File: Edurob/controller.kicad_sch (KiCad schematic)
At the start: 7 parts, among them SW1 SW_Push, U4 ESP32-S3-WROOM-1

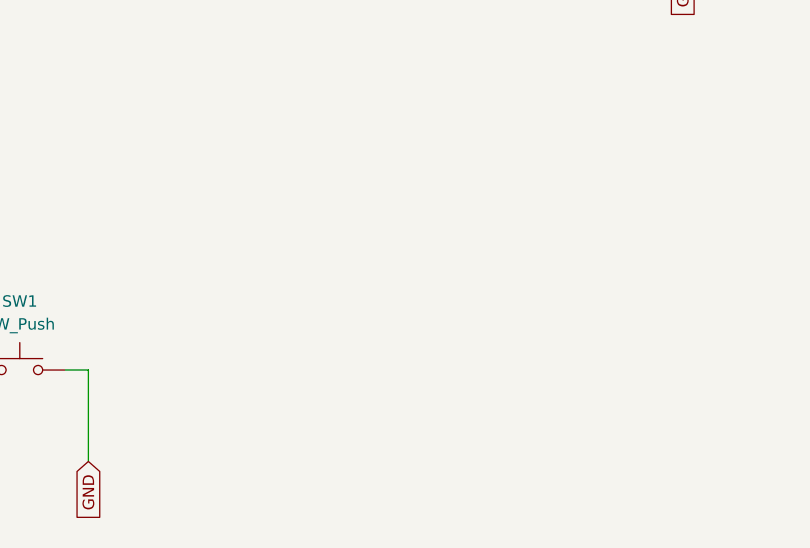
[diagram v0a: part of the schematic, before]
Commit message: Added GPIO Expander, finalized Connector positions
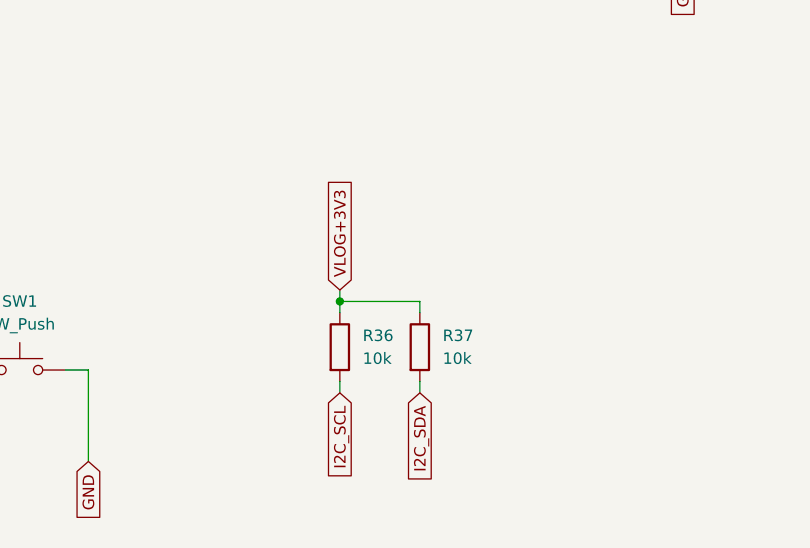
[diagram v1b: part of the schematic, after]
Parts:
- added R36, R37: 10k, Resistor_SMD:R_0603_1608Metric, symbol Device:R
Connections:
- net I2C_SCL: now also R36.2
- net I2C_SDA: now also R37.2
- net VLOG+3V3: now also R36.1, R37.1
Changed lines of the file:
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@@
 (kicad_sch (version 20230121) (generator eeschema)
   (paper "A4")
+  (junction (at 101.6 170.18) (diameter 0) (color 0 0 0 0)
+  )
   (junction (at 17.78 177.8) (diameter 0) (color 0 0 0 0)
   )
@@
     (stroke (width 0) (type default))
   )
+  (wire (pts (xy 101.6 168.91) (xy 101.6 170.18))
+    (stroke (width 0) (type default))
+  )
   (wire (pts (xy 185.42 104.14) (xy 186.69 104.14))
     (stroke (width 0) (type default))
@@
     (stroke (width 0) (type default))
   )
+  (wire (pts (xy 110.49 180.34) (xy 110.49 179.07))
+    (stroke (width 0) (type default))
+  )
   (wire (pts (xy 17.78 186.69) (xy 17.78 187.96))
     (stroke (width 0) (type default))
@@
     (stroke (width 0) (type default))
   )
+  (wire (pts (xy 110.49 171.45) (xy 110.49 170.18))
+    (stroke (width 0) (type default))
+  )
   (wire (pts (xy 185.42 124.46) (xy 186.69 124.46))
     (stroke (width 0) (type default))
@@
     (stroke (width 0) (type default))
   )
+  (wire (pts (xy 101.6 170.18) (xy 101.6 171.45))
+    (stroke (width 0) (type default))
+  )
   (wire (pts (xy 26.67 177.8) (xy 17.78 177.8))
     (stroke (width 0) (type default))
@@
     (stroke (width 0) (type default))
   )
+  (wire (pts (xy 101.6 180.34) (xy 101.6 179.07))
+    (stroke (width 0) (type default))
+  )
   (wire (pts (xy 186.69 53.34) (xy 185.42 53.34))
     (stroke (width 0) (type default))
@@
   )
   (wire (pts (xy 185.42 73.66) (xy 186.69 73.66))
+    (stroke (width 0) (type default))
+  )
+  (wire (pts (xy 110.49 170.18) (xy 101.6 170.18))
     (stroke (width 0) (type default))
   )
@@
     )
   )
+  (global_label "VLOG+3V3" (shape input) (at 101.6 168.91 90) (fields_autoplaced)
+    (effects (font (size 1.27 1.27)) (justify left))
+    (property "Intersheetrefs" "${INTERSHEET_REFS}" (at 101.6 156.1276 90)
+      (effects (font (size 1.27 1.27)) (justify left) hide)
+    )
+  )
+  (global_label "I2C_SDA" (shape input) (at 110.49 180.34 270) (fields_autoplaced)
+    (effects (font (size 1.27 1.27)) (justify right))
+    (property "Intersheetrefs" "${INTERSHEET_REFS}" (at 110.49 190.9452 90)
+      (effects (font (size 1.27 1.27)) (justify right) hide)
+    )
+  )
   (global_label "MOT_B_ENCA" (shape input) (at 186.69 81.28 0) (fields_autoplaced)
     (effects (font (size 1.27 1.27)) (justify left))
@@
     )
   )
+  (global_label "I2C_SCL" (shape input) (at 101.6 180.34 270) (fields_autoplaced)
+    (effects (font (size 1.27 1.27)) (justify right))
+    (property "Intersheetrefs" "${INTERSHEET_REFS}" (at 101.6 190.8847 90)
+      (effects (font (size 1.27 1.27)) (justify right) hide)
+    )
+  )
   (global_label "EspEn" (shape input) (at 26.67 171.45 90) (fields_autoplaced)
     (effects (font (size 1.27 1.27)) (justify left))
@@
     (property "Intersheetrefs" "${INTERSHEET_REFS}" (at 84.6726 53.4194 0)
       (effects (font (size 1.27 1.27)) (justify right) hide)
+    )
+  )
+  (symbol (lib_id "Device:R") (at 101.6 175.26 0) (unit 1)
+    (in_bom yes) (on_board yes) (dnp no) (fields_autoplaced)
+    (property "Reference" "R36" (at 104.14 173.9899 0)
+      (effects (font (size 1.27 1.27)) (justify left))
+    )
+    (property "Value" "10k" (at 104.14 176.5299 0)
+      (effects (font (size 1.27 1.27)) (justify left))
+    )
+    (property "Footprint" "Resistor_SMD:R_0603_1608Metric" (at 99.822 175.26 90)
+      (effects (font (size 1.27 1.27)) hide)
+    )
+    (property "Datasheet" "~" (at 101.6 175.26 0)
+      (effects (font (size 1.27 1.27)) hide)
+    )
+    (pin "1")
+    (pin "2")
+    (instances
+      (project "Edurob"
+        (path "/ea495553-3cd2-4380-af57-b7ab16ec3dc9/8aa2f8b0-d8d3-42d6-a936-678d5127e1c2"
+          (reference "R36") (unit 1)
+        )
+      )
     )
   )
@@
       )
       (project "Edurob"
-        (path "/ea495553-3cd2-4380-af57-b7ab16ec3dc9"
-          (reference "C1") (unit 1)
-        )
         (path "/ea495553-3cd2-4380-af57-b7ab16ec3dc9/8aa2f8b0-d8d3-42d6-a936-678d5127e1c2"
           (reference "C8") (unit 1)
@@
       )
       (project "Edurob"
-        (path "/ea495553-3cd2-4380-af57-b7ab16ec3dc9"
-          (reference "R1") (unit 1)
-        )
         (path "/ea495553-3cd2-4380-af57-b7ab16ec3dc9/8aa2f8b0-d8d3-42d6-a936-678d5127e1c2"
           (reference "R4") (unit 1)
@@
       )
       (project "Edurob"
-        (path "/ea495553-3cd2-4380-af57-b7ab16ec3dc9"
-          (reference "C1") (unit 1)
-        )
         (path "/ea495553-3cd2-4380-af57-b7ab16ec3dc9/8aa2f8b0-d8d3-42d6-a936-678d5127e1c2"
           (reference "C2") (unit 1)
@@
       )
       (project "Edurob"
-        (path "/ea495553-3cd2-4380-af57-b7ab16ec3dc9"
-          (reference "R1") (unit 1)
-        )
         (path "/ea495553-3cd2-4380-af57-b7ab16ec3dc9/8aa2f8b0-d8d3-42d6-a936-678d5127e1c2"
           (reference "R2") (unit 1)
+        )
+      )
+    )
+  )
+  (symbol (lib_id "Device:R") (at 110.49 175.26 0) (unit 1)
+    (in_bom yes) (on_board yes) (dnp no) (fields_autoplaced)
+    (property "Reference" "R37" (at 113.03 173.9899 0)
+      (effects (font (size 1.27 1.27)) (justify left))
+    )
+    (property "Value" "10k" (at 113.03 176.5299 0)
+      (effects (font (size 1.27 1.27)) (justify left))
+    )
+    (property "Footprint" "Resistor_SMD:R_0603_1608Metric" (at 108.712 175.26 90)
+      (effects (font (size 1.27 1.27)) hide)
+    )
+    (property "Datasheet" "~" (at 110.49 175.26 0)
+      (effects (font (size 1.27 1.27)) hide)
+    )
+    (pin "1")
+    (pin "2")
+    (instances
+      (project "Edurob"
+        (path "/ea495553-3cd2-4380-af57-b7ab16ec3dc9/8aa2f8b0-d8d3-42d6-a936-678d5127e1c2"
+          (reference "R37") (unit 1)
         )
       )
@@
       )
       (project "Edurob"
-        (path "/ea495553-3cd2-4380-af57-b7ab16ec3dc9"
-          (reference "SW1") (unit 1)
-        )
         (path "/ea495553-3cd2-4380-af57-b7ab16ec3dc9/8aa2f8b0-d8d3-42d6-a936-678d5127e1c2"
           (reference "SW1") (unit 1)
@@
       )
       (project "Edurob"
-        (path "/ea495553-3cd2-4380-af57-b7ab16ec3dc9"
-          (reference "SW1") (unit 1)
-        )
         (path "/ea495553-3cd2-4380-af57-b7ab16ec3dc9/8aa2f8b0-d8d3-42d6-a936-678d5127e1c2"
           (reference "SW2") (unit 1)

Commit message: Finalized part placement
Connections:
- net DXL_RXD: now also U4.8 (GPIO15/U0RTS/ADC2_CH4/XTAL_32K_P); no longer U4.9 (GPIO16/U0CTS/ADC2_CH5/XTAL_32K_N)
- net DXL_TXD: now also U4.9 (GPIO16/U0CTS/ADC2_CH5/XTAL_32K_N); no longer U4.8 (GPIO15/U0RTS/ADC2_CH4/XTAL_32K_P)
- net MOT_A_PWM: now also U4.25 (GPIO48/SPICLK_N/SUBSPICLK_N_DIFF); no longer U4.32 (MTCK/GPIO39/CLK_OUT3/SUBSPICS1)
- net MOT_B_ENCA: now also U4.34 (MTDI/GPIO41/CLK_OUT1); no longer U4.5 (GPIO5/TOUCH5/ADC1_CH4)
- net MOT_B_ENCB: now also U4.35 (MTMS/GPIO42); no longer U4.4 (GPIO4/TOUCH4/ADC1_CH3)
- net MOT_B_PWM: now also U4.32 (MTCK/GPIO39/CLK_OUT3/SUBSPICS1); no longer U4.35 (MTMS/GPIO42)
- net MOT_C_PWM: now also U4.22 (GPIO14/TOUCH14/ADC2_CH3/FSPIWP/FSPIDQS/SUBSPIWP); no longer U4.34 (MTDI/GPIO41/CLK_OUT1)
- net MOT_D_ENCA: now also U4.4 (GPIO4/TOUCH4/ADC1_CH3); no longer U4.10 (GPIO17/U1TXD/ADC2_CH6)
- net MOT_D_ENCB: now also U4.5 (GPIO5/TOUCH5/ADC1_CH4); no longer U4.22 (GPIO14/TOUCH14/ADC2_CH3/FSPIWP/FSPIDQS/SUBSPIWP)
- net MOT_D_PWM: now also U4.10 (GPIO17/U1TXD/ADC2_CH6); no longer U4.33 (MTDO/GPIO40/CLK_OUT2)
- net MOT_STBY: now also U4.33 (MTDO/GPIO40/CLK_OUT2); no longer U4.25 (GPIO48/SPICLK_N/SUBSPICLK_N_DIFF)

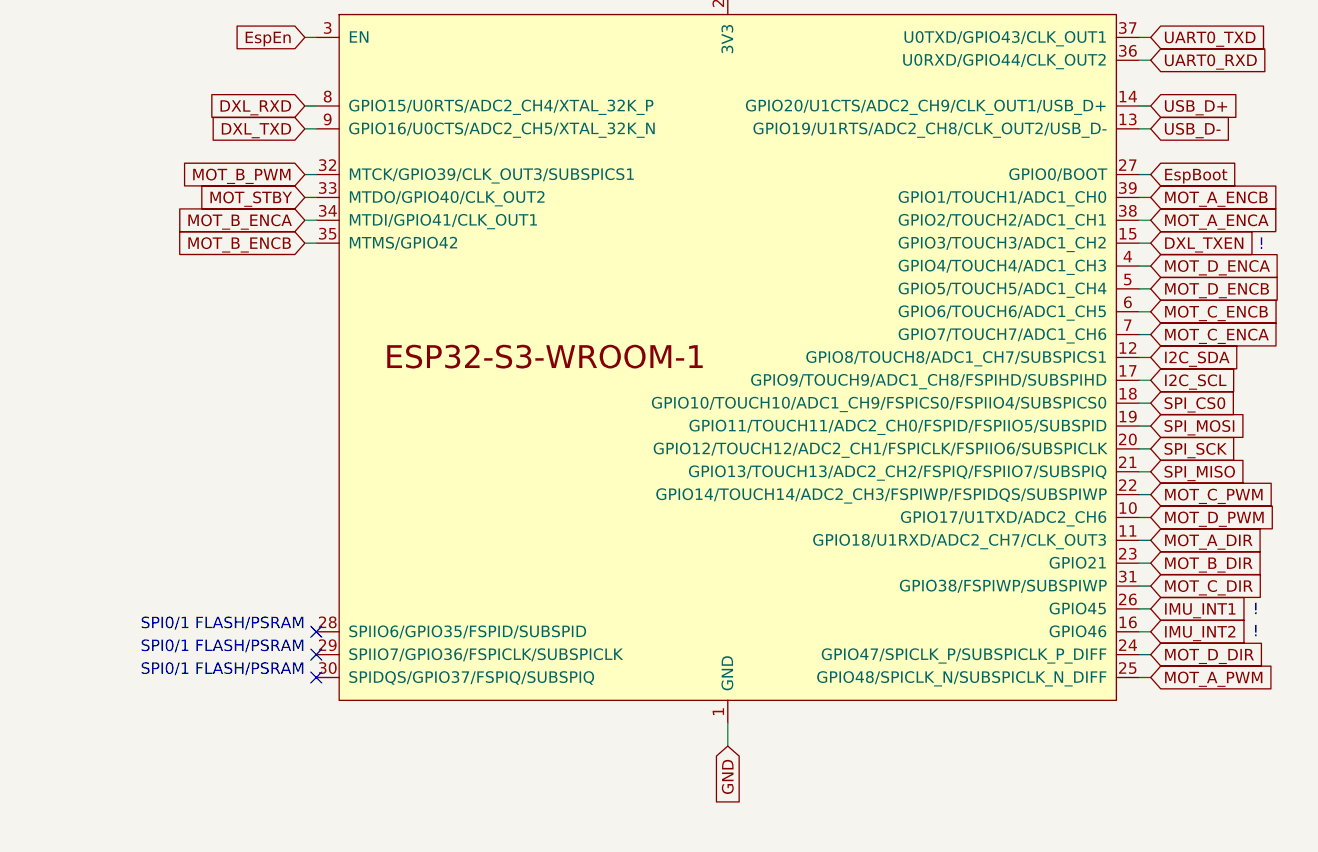
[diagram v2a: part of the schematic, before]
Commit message: Finished routing and part placement
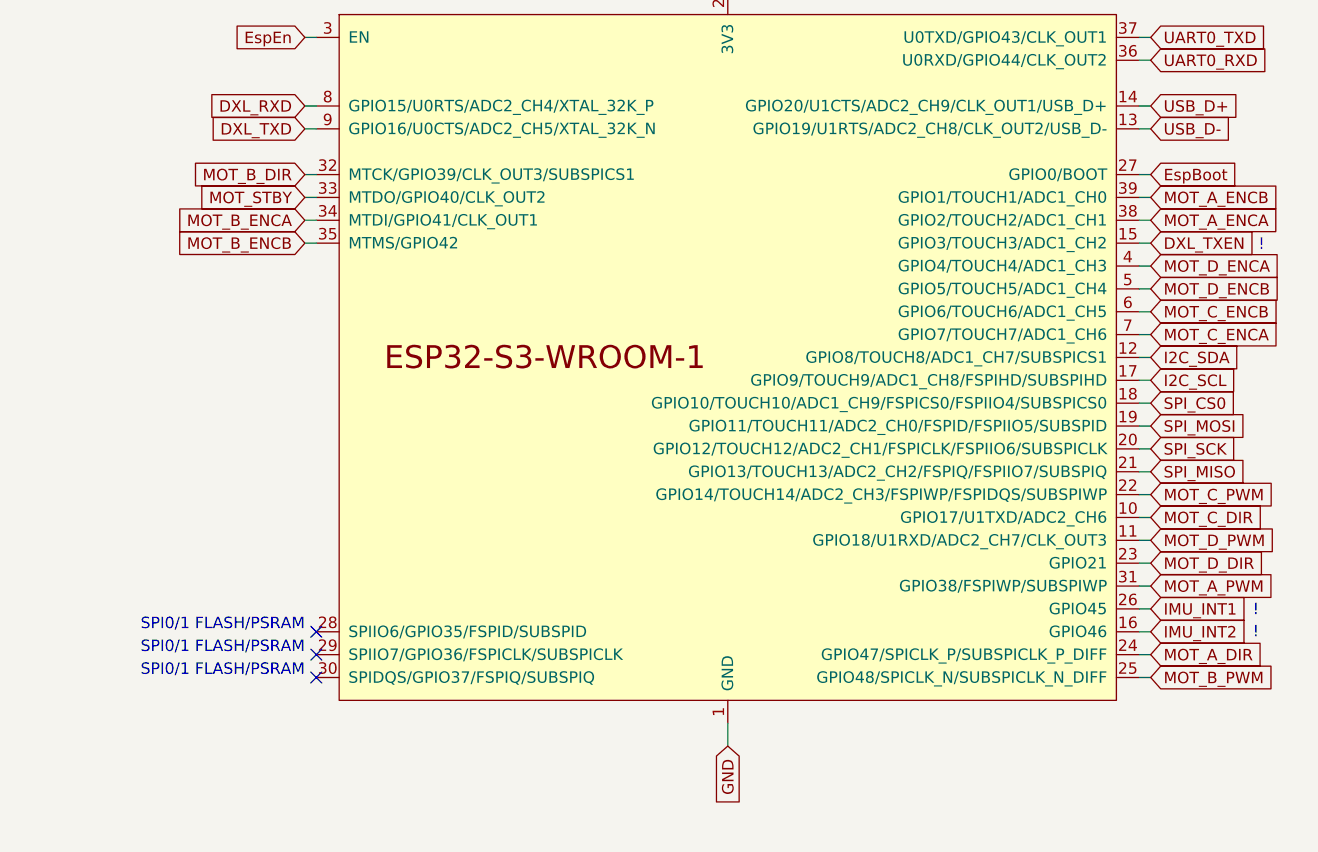
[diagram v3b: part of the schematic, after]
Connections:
- net MOT_A_DIR: now also U4.24 (GPIO47/SPICLK_P/SUBSPICLK_P_DIFF); no longer U4.11 (GPIO18/U1RXD/ADC2_CH7/CLK_OUT3)
- net MOT_A_PWM: now also U4.31 (GPIO38/FSPIWP/SUBSPIWP); no longer U4.25 (GPIO48/SPICLK_N/SUBSPICLK_N_DIFF)
- net MOT_B_DIR: now also U4.32 (MTCK/GPIO39/CLK_OUT3/SUBSPICS1); no longer U4.23 (GPIO21)
- net MOT_B_PWM: now also U4.25 (GPIO48/SPICLK_N/SUBSPICLK_N_DIFF); no longer U4.32 (MTCK/GPIO39/CLK_OUT3/SUBSPICS1)
- net MOT_C_DIR: now also U4.10 (GPIO17/U1TXD/ADC2_CH6); no longer U4.31 (GPIO38/FSPIWP/SUBSPIWP)
- net MOT_D_DIR: now also U4.23 (GPIO21); no longer U4.24 (GPIO47/SPICLK_P/SUBSPICLK_P_DIFF)
- net MOT_D_PWM: now also U4.11 (GPIO18/U1RXD/ADC2_CH7/CLK_OUT3); no longer U4.10 (GPIO17/U1TXD/ADC2_CH6)

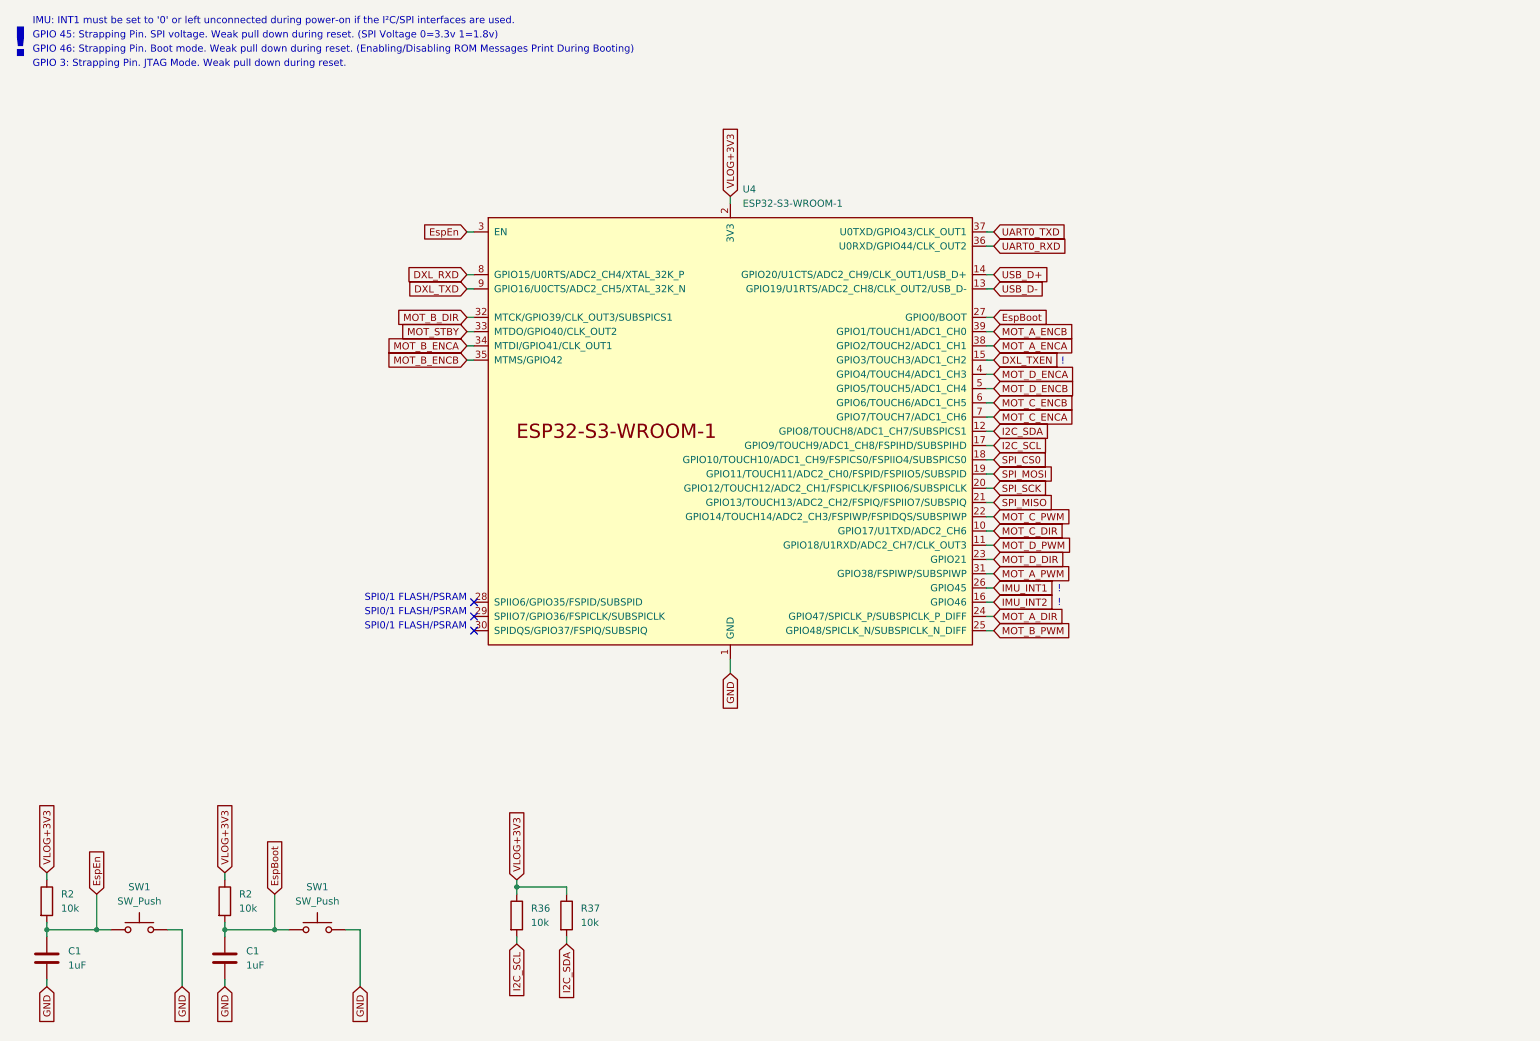
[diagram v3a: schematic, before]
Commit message: Finished silkscreen + fixed board outline
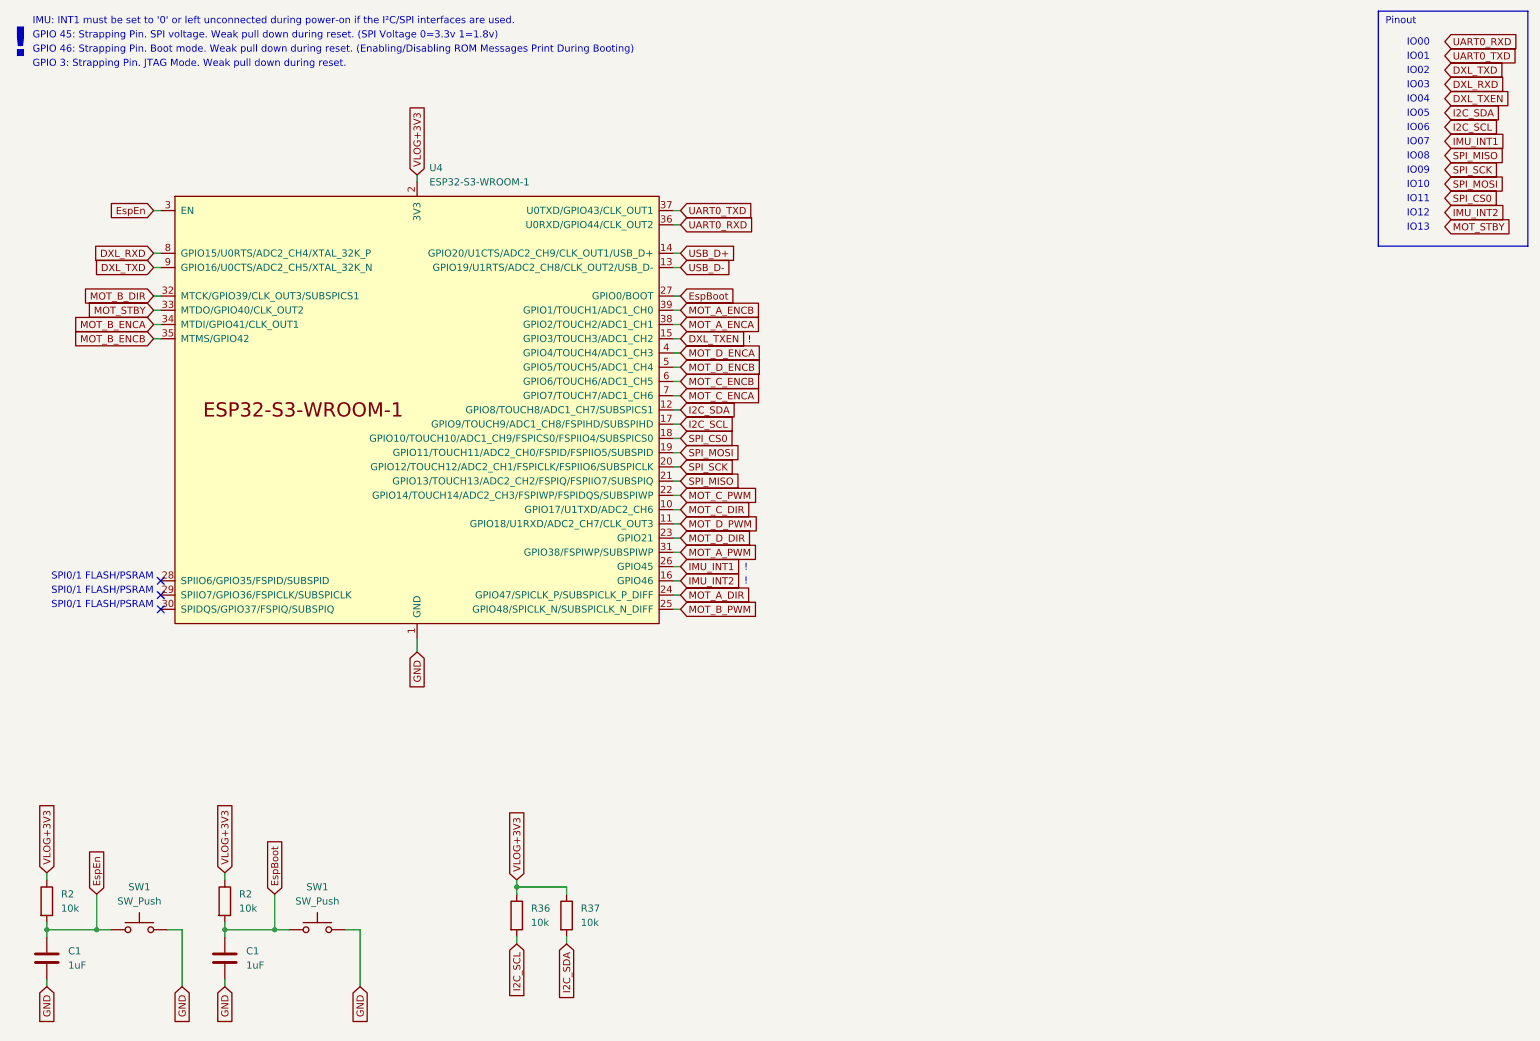
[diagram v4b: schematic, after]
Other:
- note added: "IO00"
- note added: "IO01"
- note added: "IO02"
- note added: "IO03"
- note added: "IO04"
- note added: "IO05"
- note added: "IO06"
- note added: "IO07"
- note added: "IO08"
- note added: "IO09"
- note added: "IO10"
- note added: "IO11"
- note added: "IO12"
- note added: "IO13"
- note added: "Pinout"
- moved on the sheet: U4
